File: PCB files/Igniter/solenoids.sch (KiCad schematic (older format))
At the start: 15 parts, among them Q2 N MOSFET, Q3 N MOSFET, Q4 N MOSFET, Q5 N MOSFET, Q6 N MOSFET

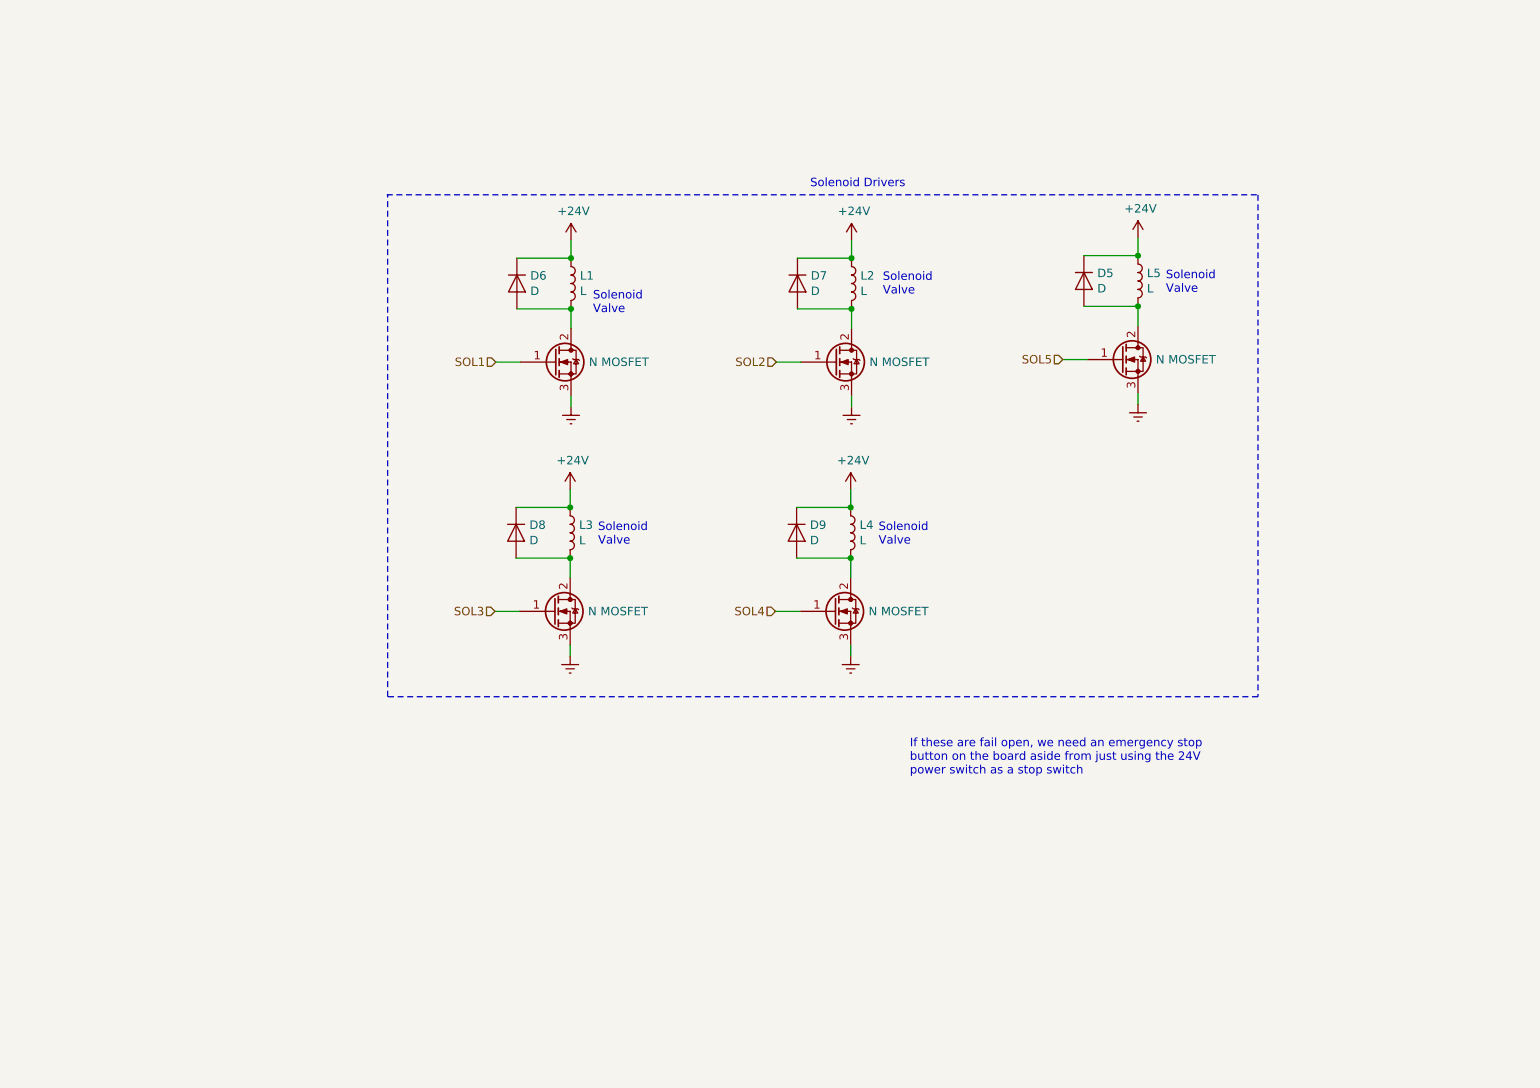
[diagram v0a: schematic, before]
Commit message: 11/13/2019
-Began adding control switches to schematic
-Arranged schematic to group inputs and outputs
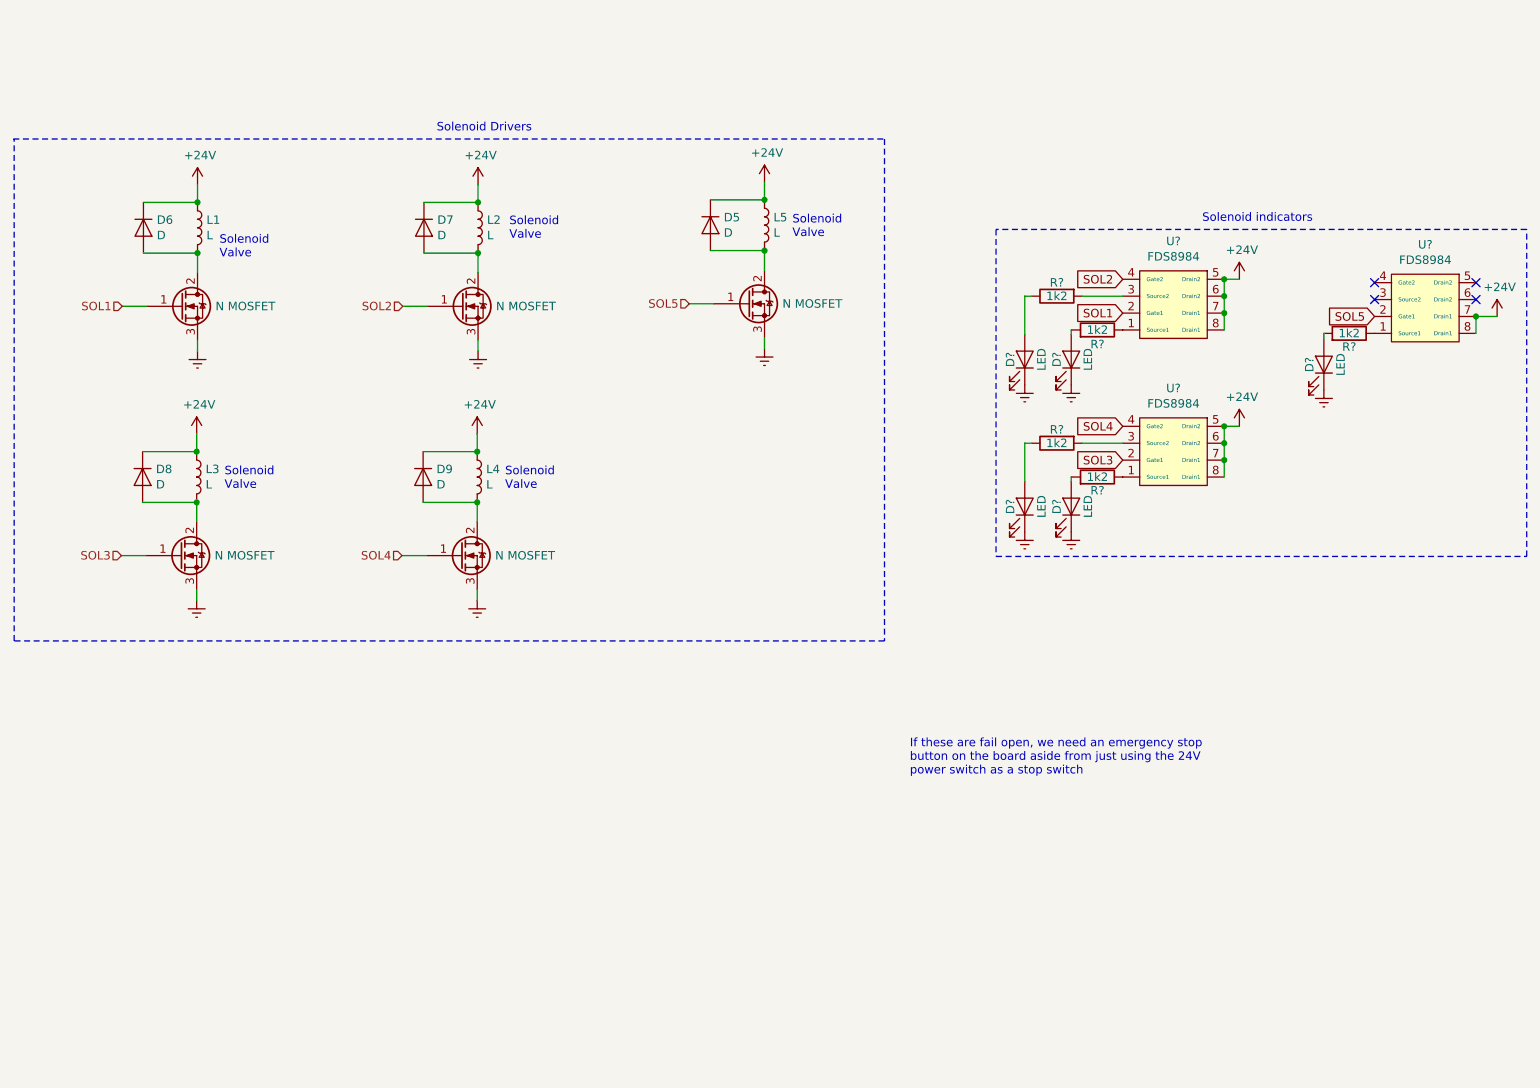
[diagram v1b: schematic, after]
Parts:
- added D? (x5): LED, LED_SMD:LED_1206_3216Metric, symbol Device:LED
- added R? (x5): 1k2, Resistor_SMD:R_1210_3225Metric, symbol Device:R
- added U? (x3): FDS8984, Package_SO:SO-8_5.3x6.2mm_P1.27mm, symbol Igniter-rescue:FDS8984
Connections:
- net +24V: now also U?.5 (Drain2), U?.5 (Drain2), U?.6 (Drain2), U?.6 (Drain2), U?.7 (Drain1), U?.7 (Drain1), U?.7 (Drain1), U?.8 (Drain1), U?.8 (Drain1), U?.8 (Drain1)
- net GNDREF: now also D?.1 (K), D?.1 (K), D?.1 (K), D?.1 (K), D?.1 (K)
- net SOL1: now also U?.2 (Gate1)
- net SOL2: now also U?.4 (Gate2)
- net SOL3: now also U?.2 (Gate1)
- net SOL4: now also U?.4 (Gate2)
- net SOL5: now also U?.2 (Gate1)
- new net: D?.2 (A), R?.1 (x2)
- new net: R?.2, U?.3 (Source2) (x2)
- new net: D?.2 (A), R?.2 (x3)
- new net: R?.1, U?.1 (Source1) (x3)
- no-connect marks 0 -> 4
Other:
- note added: "Solenoid indicators"
- moved on the sheet: D5, D6, D7, D8, D9, L1, L2, L3, L4, L5

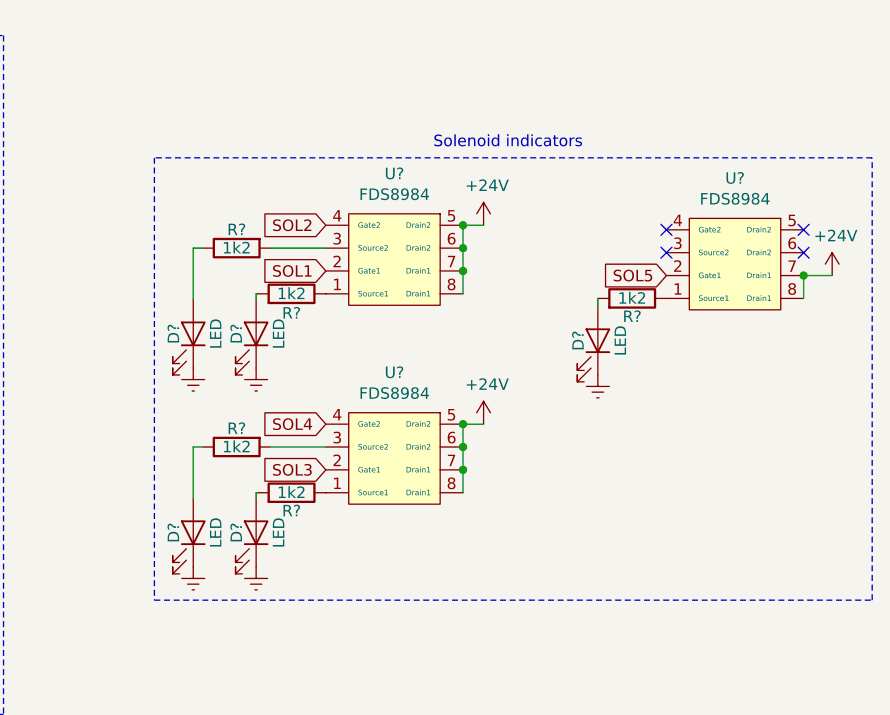
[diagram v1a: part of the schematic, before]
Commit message: 11/14/2019
-Added a couple more mounting holes to keep board from flexing when plugging in connectors
-5V regulator likely not needed with new p ducers
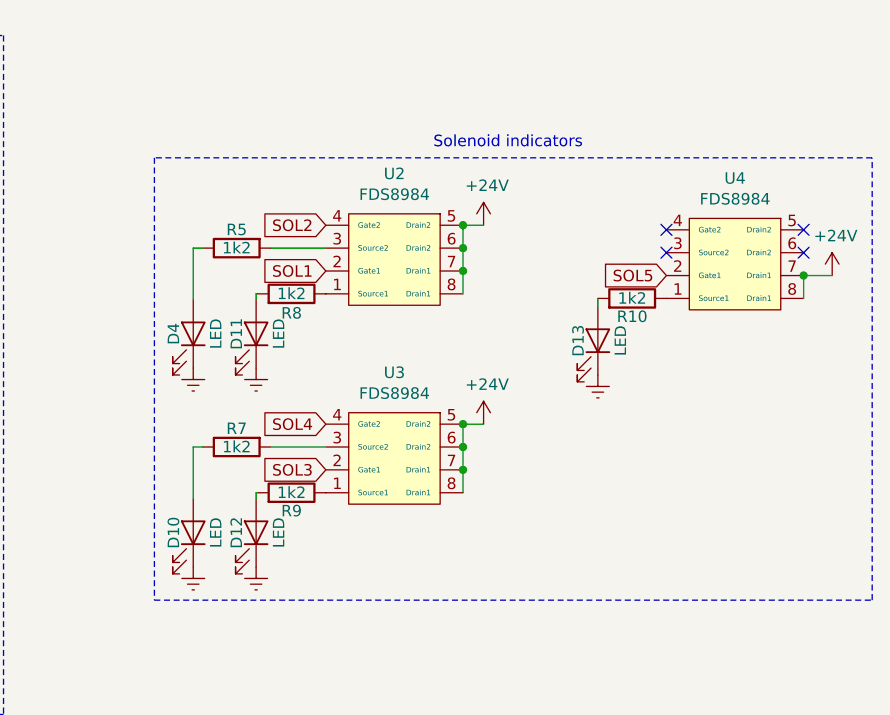
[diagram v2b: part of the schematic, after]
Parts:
- gave numbers to parts that had none: 13
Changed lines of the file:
@@
 LIBS:interface
 LIBS:Igniter-cache
-EELAYER 29 0
+EELAYER 26 0
 EELAYER END
 $Descr A4 11693 8268
@@
 $EndBitmap
 $Comp
-L Device:LED D?
+L Device:LED D4
 U 1 1 5DD6B6EC
 P 7045 3265
-AR Path="/5DB4D508/5DD6B6EC" Ref="D?"  Part="1"
+AR Path="/5DB4D508/5DD6B6EC" Ref="D4"  Part="1"
 AR Path="/5DD6B6EC" Ref="D?"  Part="1"
-F 0 "D?" H 7045 3180 50  0000 C CNN
+F 0 "D4" H 7045 3180 50  0000 C CNN
 F 1 "LED" H 7045 3365 50  0000 C CNN
 F 2 "LED_SMD:LED_1206_3216Metric" H 7045 3265 50  0001 C CNN
@@
 $EndComp
 $Comp
-L Device:R R?
+L Device:R R5
 U 1 1 5DD6B6F2
 P 7235 2890
-AR Path="/5DB4D508/5DD6B6F2" Ref="R?"  Part="1"
+AR Path="/5DB4D508/5DD6B6F2" Ref="R5"  Part="1"
 AR Path="/5DD6B6F2" Ref="R?"  Part="1"
-F 0 "R?" V 7155 2890 50  0000 C CNN
+F 0 "R5" V 7155 2890 50  0000 C CNN
 F 1 "1k2" V 7235 2890 50  0000 C CNN
 F 2 "Resistor_SMD:R_1210_3225Metric" V 7165 2890 50  0001 C CNN
@@
 $EndComp
 $Comp
-L power:GNDREF #PWR?
+L power:GNDREF #PWR017
 U 1 1 5DD6B6F8
 P 7045 3415
-AR Path="/5DB4D508/5DD6B6F8" Ref="#PWR?"  Part="1"
+AR Path="/5DB4D508/5DD6B6F8" Ref="#PWR017"  Part="1"
 AR Path="/5DD6B6F8" Ref="#PWR?"  Part="1"
-F 0 "#PWR?" H 7045 3165 50  0001 C CNN
+F 0 "#PWR017" H 7045 3165 50  0001 C CNN
 F 1 "GNDREF" H 7050 3242 50  0001 C CNN
 F 2 "" H 7045 3415 50  0001 C CNN
@@
 SOL2
 $Comp
-L Device:LED D?
+L Device:LED D11
 U 1 1 5DD6B701
 P 7320 3265
-AR Path="/5DB4D508/5DD6B701" Ref="D?"  Part="1"
+AR Path="/5DB4D508/5DD6B701" Ref="D11"  Part="1"
 AR Path="/5DD6B701" Ref="D?"  Part="1"
-F 0 "D?" H 7320 3180 50  0000 C CNN
+F 0 "D11" H 7320 3180 50  0000 C CNN
 F 1 "LED" H 7320 3365 50  0000 C CNN
 F 2 "LED_SMD:LED_1206_3216Metric" H 7320 3265 50  0001 C CNN
@@
 $EndComp
 $Comp
-L Device:R R?
+L Device:R R8
 U 1 1 5DD6B707
 P 7475 3090
-AR Path="/5DB4D508/5DD6B707" Ref="R?"  Part="1"
+AR Path="/5DB4D508/5DD6B707" Ref="R8"  Part="1"
 AR Path="/5DD6B707" Ref="R?"  Part="1"
-F 0 "R?" V 7390 3090 50  0000 C CNN
+F 0 "R8" V 7390 3090 50  0000 C CNN
 F 1 "1k2" V 7475 3090 50  0000 C CNN
 F 2 "Resistor_SMD:R_1210_3225Metric" V 7405 3090 50  0001 C CNN
@@
 $EndComp
 $Comp
-L power:GNDREF #PWR?
+L power:GNDREF #PWR040
 U 1 1 5DD6B70D
 P 7320 3415
-AR Path="/5DB4D508/5DD6B70D" Ref="#PWR?"  Part="1"
+AR Path="/5DB4D508/5DD6B70D" Ref="#PWR040"  Part="1"
 AR Path="/5DD6B70D" Ref="#PWR?"  Part="1"
-F 0 "#PWR?" H 7320 3165 50  0001 C CNN
+F 0 "#PWR040" H 7320 3165 50  0001 C CNN
 F 1 "GNDREF" H 7325 3242 50  0001 C CNN
 F 2 "" H 7320 3415 50  0001 C CNN
@@
 P 8315 2790
 AR Path="/5DD6B713" Ref="#PWR?"  Part="1"
-AR Path="/5DB4D508/5DD6B713" Ref="#PWR?"  Part="1"
-F 0 "#PWR?" H 8315 2640 50  0001 C CNN
+AR Path="/5DB4D508/5DD6B713" Ref="#PWR044"  Part="1"
+F 0 "#PWR044" H 8315 2640 50  0001 C CNN
 F 1 "+24V" H 8330 2963 50  0000 C CNN
 F 2 "" H 8315 2790 50  0001 C CNN
@@
 P 7925 2940
 AR Path="/5DD6B71A" Ref="U?"  Part="1"
-AR Path="/5DB4D508/5DD6B71A" Ref="U?"  Part="1"
-F 0 "U?" H 7925 3315 50  0000 C CNN
+AR Path="/5DB4D508/5DD6B71A" Ref="U2"  Part="1"
+F 0 "U2" H 7925 3315 50  0000 C CNN
 F 1 "FDS8984" H 7925 3224 50  0000 C CNN
 F 2 "Package_SO:SO-8_5.3x6.2mm_P1.27mm" H 7925 3040 50  0001 C CNN
@@
 Connection ~ 8225 2790
 $Comp
-L Device:LED D?
+L Device:LED D13
 U 1 1 5DD6B726
 P 8815 3295
-AR Path="/5DB4D508/5DD6B726" Ref="D?"  Part="1"
+AR Path="/5DB4D508/5DD6B726" Ref="D13"  Part="1"
 AR Path="/5DD6B726" Ref="D?"  Part="1"
-F 0 "D?" H 8815 3210 50  0000 C CNN
+F 0 "D13" H 8815 3210 50  0000 C CNN
 F 1 "LED" H 8815 3395 50  0000 C CNN
 F 2 "LED_SMD:LED_1206_3216Metric" H 8815 3295 50  0001 C CNN
@@
 $EndComp
 $Comp
-L Device:R R?
+L Device:R R10
 U 1 1 5DD6B72C
 P 8965 3110
-AR Path="/5DB4D508/5DD6B72C" Ref="R?"  Part="1"
+AR Path="/5DB4D508/5DD6B72C" Ref="R10"  Part="1"
 AR Path="/5DD6B72C" Ref="R?"  Part="1"
-F 0 "R?" V 8885 3110 50  0000 C CNN
+F 0 "R10" V 8885 3110 50  0000 C CNN
 F 1 "1k2" V 8965 3110 50  0000 C CNN
 F 2 "Resistor_SMD:R_1210_3225Metric" V 8895 3110 50  0001 C CNN
@@
 $EndComp
 $Comp
-L power:GNDREF #PWR?
+L power:GNDREF #PWR046
 U 1 1 5DD6B732
 P 8815 3445
-AR Path="/5DB4D508/5DD6B732" Ref="#PWR?"  Part="1"
+AR Path="/5DB4D508/5DD6B732" Ref="#PWR046"  Part="1"
 AR Path="/5DD6B732" Ref="#PWR?"  Part="1"
-F 0 "#PWR?" H 8815 3195 50  0001 C CNN
+F 0 "#PWR046" H 8815 3195 50  0001 C CNN
 F 1 "GNDREF" H 8820 3272 50  0001 C CNN
 F 2 "" H 8815 3445 50  0001 C CNN
@@
 P 9840 3010
 AR Path="/5DD6B738" Ref="#PWR?"  Part="1"
-AR Path="/5DB4D508/5DD6B738" Ref="#PWR?"  Part="1"
-F 0 "#PWR?" H 9840 2860 50  0001 C CNN
+AR Path="/5DB4D508/5DD6B738" Ref="#PWR047"  Part="1"
+F 0 "#PWR047" H 9840 2860 50  0001 C CNN
 F 1 "+24V" H 9855 3183 50  0000 C CNN
 F 2 "" H 9840 3010 50  0001 C CNN
@@
 P 9415 2960
 AR Path="/5DD6B73F" Ref="U?"  Part="1"
-AR Path="/5DB4D508/5DD6B73F" Ref="U?"  Part="1"
-F 0 "U?" H 9415 3335 50  0000 C CNN
+AR Path="/5DB4D508/5DD6B73F" Ref="U4"  Part="1"
+F 0 "U4" H 9415 3335 50  0000 C CNN
 F 1 "FDS8984" H 9415 3244 50  0000 C CNN
 F 2 "Package_SO:SO-8_5.3x6.2mm_P1.27mm" H 9415 3060 50  0001 C CNN
@@
 	7045 2890 7085 2890
 $Comp
-L Device:LED D?
+L Device:LED D10
 U 1 1 5DD6B752
 P 7045 4135
-AR Path="/5DB4D508/5DD6B752" Ref="D?"  Part="1"
+AR Path="/5DB4D508/5DD6B752" Ref="D10"  Part="1"
 AR Path="/5DD6B752" Ref="D?"  Part="1"
-F 0 "D?" H 7045 4050 50  0000 C CNN
+F 0 "D10" H 7045 4050 50  0000 C CNN
 F 1 "LED" H 7045 4235 50  0000 C CNN
 F 2 "LED_SMD:LED_1206_3216Metric" H 7045 4135 50  0001 C CNN
@@
 $EndComp
 $Comp
-L Device:R R?
+L Device:R R7
 U 1 1 5DD6B758
 P 7235 3760
-AR Path="/5DB4D508/5DD6B758" Ref="R?"  Part="1"
+AR Path="/5DB4D508/5DD6B758" Ref="R7"  Part="1"
 AR Path="/5DD6B758" Ref="R?"  Part="1"
-F 0 "R?" V 7155 3760 50  0000 C CNN
+F 0 "R7" V 7155 3760 50  0000 C CNN
 F 1 "1k2" V 7235 3760 50  0000 C CNN
 F 2 "Resistor_SMD:R_1210_3225Metric" V 7165 3760 50  0001 C CNN
@@
 $EndComp
 $Comp
-L power:GNDREF #PWR?
+L power:GNDREF #PWR018
 U 1 1 5DD6B75E
 P 7045 4285
-AR Path="/5DB4D508/5DD6B75E" Ref="#PWR?"  Part="1"
+AR Path="/5DB4D508/5DD6B75E" Ref="#PWR018"  Part="1"
 AR Path="/5DD6B75E" Ref="#PWR?"  Part="1"
-F 0 "#PWR?" H 7045 4035 50  0001 C CNN
+F 0 "#PWR018" H 7045 4035 50  0001 C CNN
 F 1 "GNDREF" H 7050 4112 50  0001 C CNN
 F 2 "" H 7045 4285 50  0001 C CNN
@@
 $EndComp
 $Comp
-L Device:LED D?
+L Device:LED D12
 U 1 1 5DD6B764
 P 7320 4135
-AR Path="/5DB4D508/5DD6B764" Ref="D?"  Part="1"
+AR Path="/5DB4D508/5DD6B764" Ref="D12"  Part="1"
 AR Path="/5DD6B764" Ref="D?"  Part="1"
-F 0 "D?" H 7320 4050 50  0000 C CNN
+F 0 "D12" H 7320 4050 50  0000 C CNN
 F 1 "LED" H 7320 4235 50  0000 C CNN
 F 2 "LED_SMD:LED_1206_3216Metric" H 7320 4135 50  0001 C CNN
@@
 $EndComp
 $Comp
-L Device:R R?
+L Device:R R9
 U 1 1 5DD6B76A
 P 7475 3960
-AR Path="/5DB4D508/5DD6B76A" Ref="R?"  Part="1"
+AR Path="/5DB4D508/5DD6B76A" Ref="R9"  Part="1"
 AR Path="/5DD6B76A" Ref="R?"  Part="1"
-F 0 "R?" V 7395 3960 50  0000 C CNN
+F 0 "R9" V 7395 3960 50  0000 C CNN
 F 1 "1k2" V 7475 3960 50  0000 C CNN
 F 2 "Resistor_SMD:R_1210_3225Metric" V 7405 3960 50  0001 C CNN
@@
 $EndComp
 $Comp
-L power:GNDREF #PWR?
+L power:GNDREF #PWR043
 U 1 1 5DD6B770
 P 7320 4285
-AR Path="/5DB4D508/5DD6B770" Ref="#PWR?"  Part="1"
+AR Path="/5DB4D508/5DD6B770" Ref="#PWR043"  Part="1"
 AR Path="/5DD6B770" Ref="#PWR?"  Part="1"
-F 0 "#PWR?" H 7320 4035 50  0001 C CNN
+F 0 "#PWR043" H 7320 4035 50  0001 C CNN
 F 1 "GNDREF" H 7325 4112 50  0001 C CNN
 F 2 "" H 7320 4285 50  0001 C CNN
@@
 P 8315 3660
 AR Path="/5DD6B776" Ref="#PWR?"  Part="1"
-AR Path="/5DB4D508/5DD6B776" Ref="#PWR?"  Part="1"
-F 0 "#PWR?" H 8315 3510 50  0001 C CNN
+AR Path="/5DB4D508/5DD6B776" Ref="#PWR045"  Part="1"
+F 0 "#PWR045" H 8315 3510 50  0001 C CNN
 F 1 "+24V" H 8330 3833 50  0000 C CNN
 F 2 "" H 8315 3660 50  0001 C CNN
@@
 P 7925 3810
 AR Path="/5DD6B77D" Ref="U?"  Part="1"
-AR Path="/5DB4D508/5DD6B77D" Ref="U?"  Part="1"
-F 0 "U?" H 7925 4185 50  0000 C CNN
+AR Path="/5DB4D508/5DD6B77D" Ref="U3"  Part="1"
+F 0 "U3" H 7925 4185 50  0000 C CNN
 F 1 "FDS8984" H 7925 4094 50  0000 C CNN
 F 2 "Package_SO:SO-8_5.3x6.2mm_P1.27mm" H 7925 3910 50  0001 C CNN

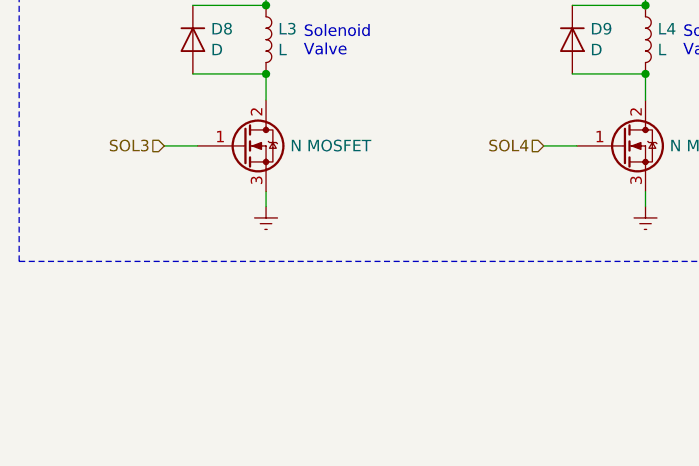
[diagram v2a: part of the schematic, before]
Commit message: 11/14/2019
-Removed 5V rail, no more 5V being used on this board
-Removed some global labels, replaced with wire connections or local net labels
-Added ignition coil primary flyback
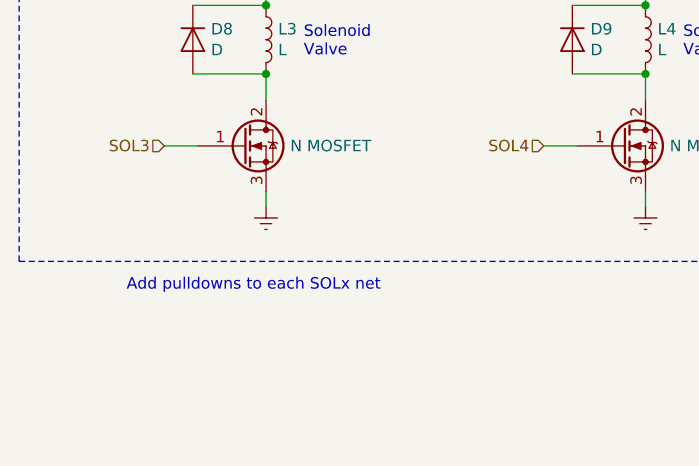
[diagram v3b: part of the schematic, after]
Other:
- note added: "Add pulldowns to each SOLx net"
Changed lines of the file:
@@
 Connection ~ 8225 3760
 Connection ~ 8225 3660
+Text Notes 1535 5065 0    50   ~ 0
+Add pulldowns to each SOLx net
 $EndSCHEMATC
